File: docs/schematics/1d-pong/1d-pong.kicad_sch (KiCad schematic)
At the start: 17 parts, among them J1 USB_B_Micro, Q2 BSS138, Q3 BSS138, SW1 SW_Push_LED, SW2 SW_Push_LED, U1 esp32-wemos-d1-mini

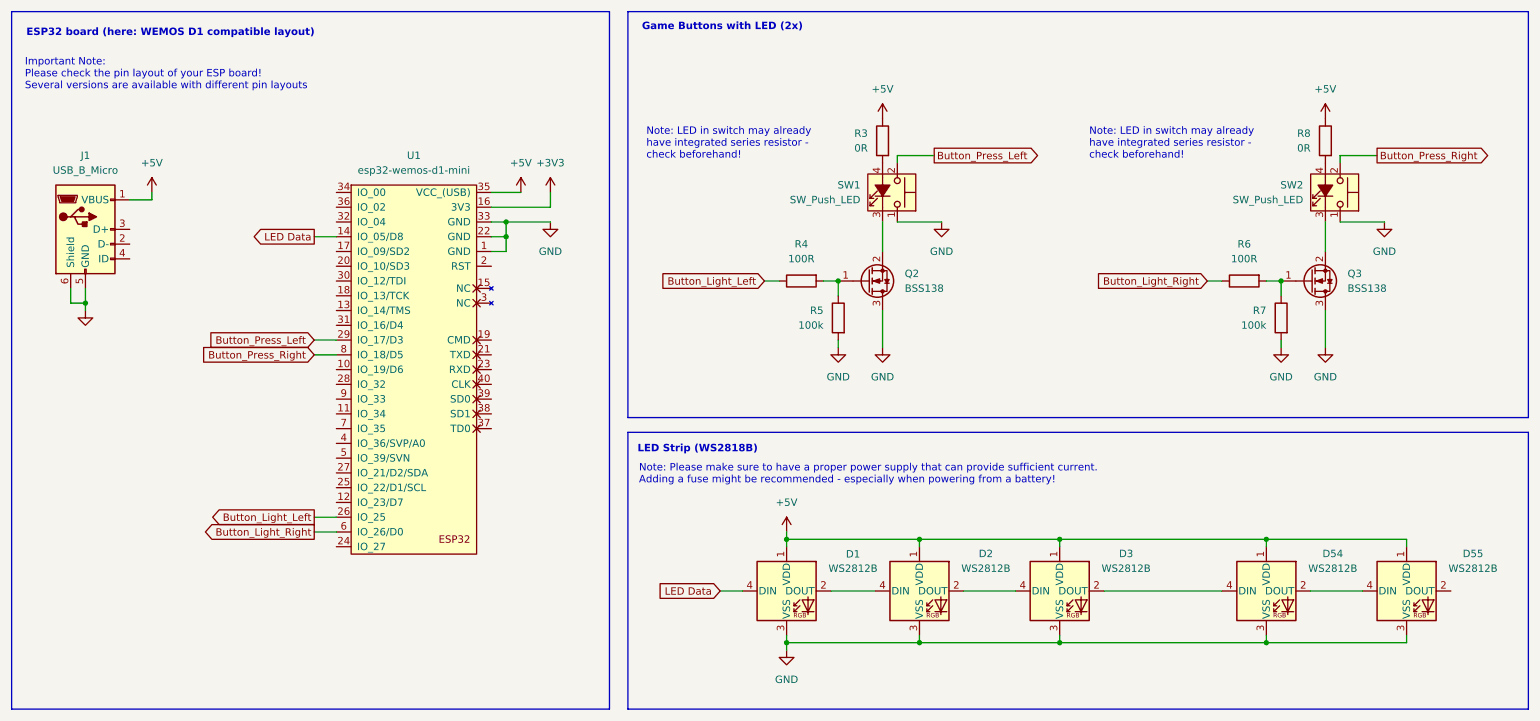
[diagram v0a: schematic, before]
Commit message: Update schematic with comments and revised part numbering
Regenerated PNG from updated SVG with white background.

Co-Authored-By: Claude Sonnet 4.5 <noreply@anthropic.com>
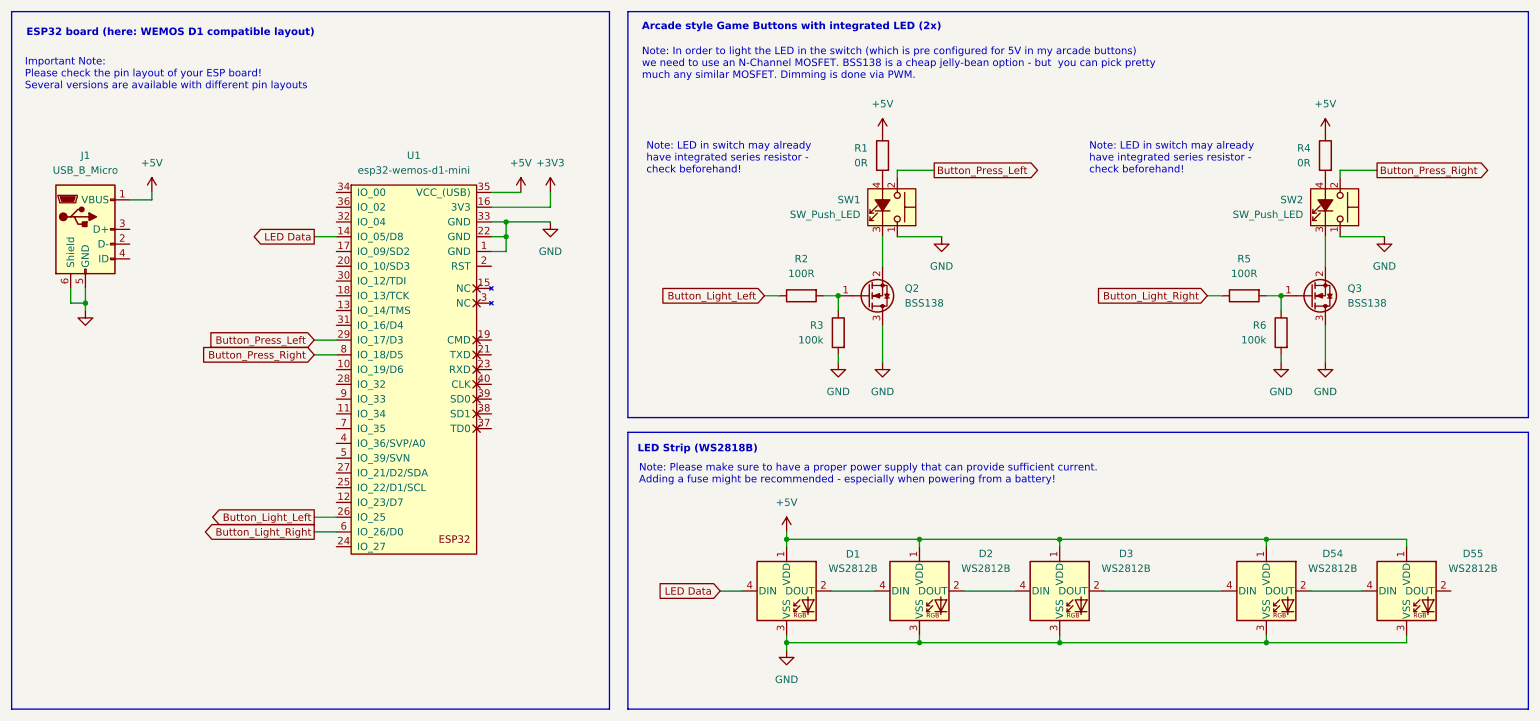
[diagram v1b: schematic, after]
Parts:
- renumbered R3 to R1, R4 to R2, R5 to R3, R8 to R4, R6 to R5, R7 to R6
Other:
- note added: "Arcade style Game Buttons with integrated LED (2x)"
- note added: "Note: In order to light the LED in the switch (which is pre configured for 5V in my arcade buttons) we need to use an N-Channel MOSFET. BSS138 is a cheap jelly-bean option - but you can pick pretty much any similar MOSFET. Dimming is done via PWM."
- note removed: "Game Buttons with LED (2x)"
- moved on the sheet: Q2, Q3, R1, R2, R3, R4, R5, R6, SW1, SW2
